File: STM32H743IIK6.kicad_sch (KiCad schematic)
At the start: 66 parts, among them Q2 MMBT3904, Q3 MMBT3904, SW1 SW_Push, SW2 SW_Push, SW3 SW_Push, SW4 SW_Push, U11 TLV75733PDBV, U2 STM32H743IITx, U8 TLV75733PDBV, Y1 25MHz, Y2 32.768KHz

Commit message: not yet
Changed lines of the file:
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@@
 	(hierarchical_label "DBG_RX"
 		(shape input)
-		(at 300.99 96.52 0)
+		(at 181.61 140.97 0)
 		(fields_autoplaced yes)
 		(effects
@@
 	(hierarchical_label "DBG_TX"
 		(shape output)
-		(at 300.99 93.98 0)
-		(fields_autoplaced yes)
-		(effects
+		(at 181.61 138.43 0)
+		(fields_autoplaced yes)
+		(effects

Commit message: Button, LED, i2s audio, LCD & SD ctrl left
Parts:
- added NT1, NT2, NT3: NetTie_2, NetTie:NetTie-2_SMD_Pad0.5mm, symbol Device:NetTie_2
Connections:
- net BCK is gone; now on net I2S_CK: U2.139 (PC10)
- net LRCK is gone; now on net LCD_BLK: U2.138 (PA15)
- net DBG_RX: now also U2.150 (PD6)
- net DBG_TX: now also U2.147 (PD5)
- net DCMI_HSYNC: now also U2.85 (PH8)
- net DCMI_PIXCLK: now also NT1.2
- net DCMI_VSYNC: now also U2.174 (PI5)
- net I2S_CK: no longer U2.51 (PA5)
- net I2S_SDO: now also U2.141 (PC12); no longer U2.151 (PD7)
- net LCD_BLK: no longer U2.163 (PB5)
- net LCD_CS: now also U2.132 (PI1), U2.7 (PI8)
- net LCD_DISP: now also U2.131 (PI0)
- net SD_DET: now also U2.2 (PE3)
- net LCD_SPI_CLK: now reaches U2.1 (PE2)
- net USART6_TX: now reaches U2.115 (PC6)
- net USART6_TX: now also NT2.1
- net USART6_RX: now reaches U2.116 (PC7)
- net USART6_RX: now also NT3.1
- net DCMI_D4: now reaches U2.129 (PH14)
- net DCMI_D5: now reaches U2.145 (PD3)
- net DCMI_D6: now reaches U2.175 (PI6)
- net DCMI_D7: now reaches U2.176 (PI7)
- net LCD_SPI_DAT: now reaches U2.5 (PE6)
- net LCD_SPI_MISO: now reaches U2.52 (PA6)
- net LCD_SPI_MISO: now also NT1.1
- net DCMI_D2: now reaches U2.88 (PH11)
- net DCMI_D3: now reaches U2.89 (PH12)
- new net DCMI_D0: NT2.2
- new net DCMI_D1: NT3.2
- new net LCD_SPI_MOSI: U2.163 (PB5)
- new net LCD_SPI_RESET: U2.151 (PD7)
- new net LCD_SPI_SCK: U2.51 (PA5)
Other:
- note added: "I2S3_CK > PC10"
- note added: "I2S3_SDO > PC12"
- note added: "I2S3_WS > PA4"
- moved on the sheet: BT2, C25, C26, C60, C61, C62, D11, D12, D7, R39, R40, R41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

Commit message: Almost finished
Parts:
- BT2: JLCPCB Part # (none) -> C964729
- Q2, Q3: JLCPCB Part # (none) -> C20526
- R22, R39: JLCPCB Part # C25741 -> C60491
- R50, R52: JLCPCB Part # C25741 -> C25744
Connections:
- net LCD_CS: no longer U2.7 (PI8)
- net LCD_SPI_DC: now also U2.134 (PI3)
- new net LCD_SPI_CS: U2.7 (PI8)
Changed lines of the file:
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@@
 		)
 	)
+	(hierarchical_label "LCD_SPI_CS"
+		(shape output)
+		(at 58.42 93.98 180)
+		(fields_autoplaced yes)
+		(effects
+			(font
+				(size 1.27 1.27)
+			)
+			(justify right)
+		)
+	)
 	(hierarchical_label "LCD_CS"
 		(shape input)
@@
 	(hierarchical_label "LCD_SPI_DC"
 		(shape output)
-		(at 234.95 86.36 180)
+		(at 58.42 81.28 180)
 		(fields_autoplaced yes)
 		(effects
@@
 		)
 	)
-	(hierarchical_label "LCD_CS"
-		(shape output)
-		(at 58.42 93.98 180)
-		(fields_autoplaced yes)
-		(effects
-			(font
-				(size 1.27 1.27)
-			)
-			(justify right)
-		)
-	)
 	(hierarchical_label "LCD_SPI_MISO"
 		(shape input)
@@
 			)
 		)
-		(property "JLCPCB Part #" "C25741"
+		(property "JLCPCB Part #" "C25744"
 			(at 252.73 266.7 0)
 			(effects
@@
 			)
 		)
+		(property "JLCPCB Part #" "C20526"
+			(at 264.16 212.09 0)
+			(effects
+				(font
+					(size 1.27 1.27)
+				)
+				(hide yes)
+			)
+		)
 		(pin "2"
 		)
@@
 			)
 		)
-		(property "JLCPCB Part #" "C25741"
+		(property "JLCPCB Part #" "C60491"
 			(at 308.61 124.46 0)
 			(effects
@@
 			)
 		)
-		(property "JLCPCB Part #" "C25741"
+		(property "JLCPCB Part #" "C25744"
 			(at 252.73 215.9 0)
 			(effects
@@
 			)
 		)
-		(property "JLCPCB Part #" "C25741"
+		(property "JLCPCB Part #" "C60491"
 			(at 308.61 168.91 0)
 			(effects
@@
 			)
 		)
+		(property "JLCPCB Part #" "C20526"
+			(at 264.16 262.89 0)
+			(effects
+				(font
+					(size 1.27 1.27)
+				)
+				(hide yes)
+			)
+		)
 		(pin "2"
 		)
@@
 				(hide yes)
 			)
+		)
+		(property "JLCPCB Part #" "C964729"
+			(at 207.01 54.61 0)
+			(effects
+				(font
+					(size 1.27 1.27)
+				)
+				(hide yes)
+			)

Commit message: Still on progress...
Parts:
- removed C45: 10uF/0805, Capacitor_SMD:C_0805_2012Metric, symbol Device:C
- removed D3: NSR0320MW2T1G, Diode_SMD:D_SOD-323, symbol Diode:NSR0340HT1G
- removed R22: 100K, Resistor_SMD:R_0402_1005Metric, symbol Device:R_Small
- removed R40: 10K, Resistor_SMD:R_0402_1005Metric, symbol Device:R_Small
- removed U11: TLV75733PDBV, Package_TO_SOT_SMD:SOT-23-5, symbol Regulator_Linear:TLV75733PDBV
- added U13: AMS1117-3.3, Package_TO_SOT_SMD:SOT-223-3_TabPin2, symbol Regulator_Linear:AMS1117-3.3
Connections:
- net +3V3: no longer C62.1, R41.1
- net BTN0: now also U2.99 (PD11)
- net BTN1: now also U2.84 (PH7)
- net GND: now also U13.1 (GND)
- net LCD_SPI_DC: now also U2.121 (PA10); no longer U2.134 (PI3)
- net LED_0: now also U2.55 (PC5)
- net LED_1: now also U2.83 (PH6)
- net VDD: now also U13.3 (VI)
- net I2S3_SD_MODE: now reaches U2.34 (PC2_C)
- net I2S2_WS: now reaches U2.92 (PB12)
- net I2S2_CK: now reaches U2.93 (PB13)
- net I2S_CK renamed I2S3_CK
- net I2S_SDO renamed I2S3_SDO
- net I2S_WS renamed I2S3_WS
- new net +3V3A: C62.1, R41.1, U13.2 (VO)
- new net I2S2_DIN: U2.134 (PI3)
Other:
- moved on the sheet: C60, C61, C62, D11, R39

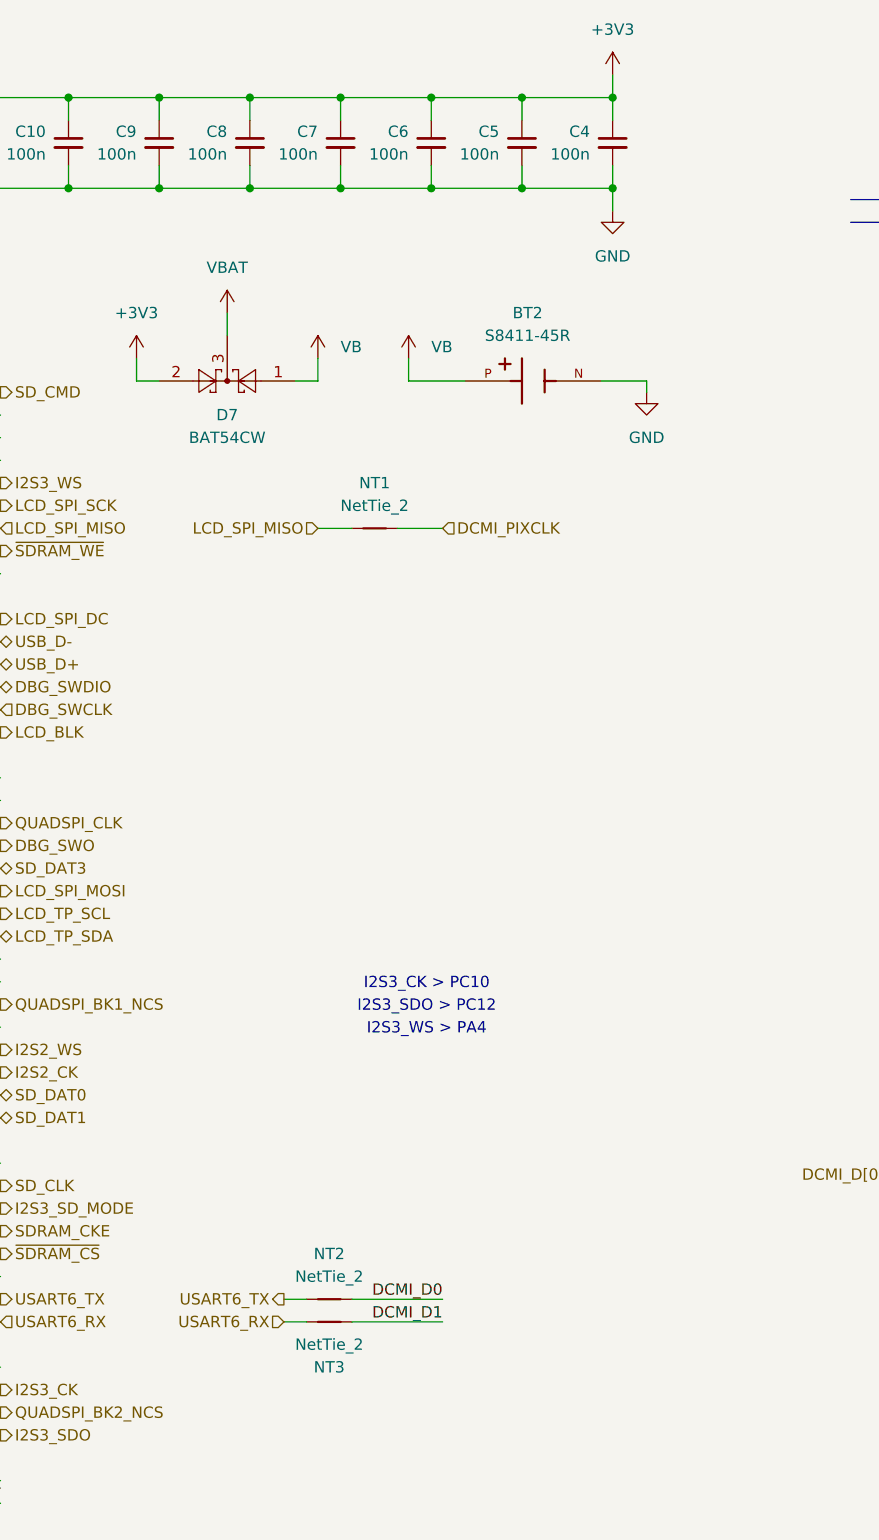
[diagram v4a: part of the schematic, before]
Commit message: Removing Camera, create alternative footprint for SPI LCD conn
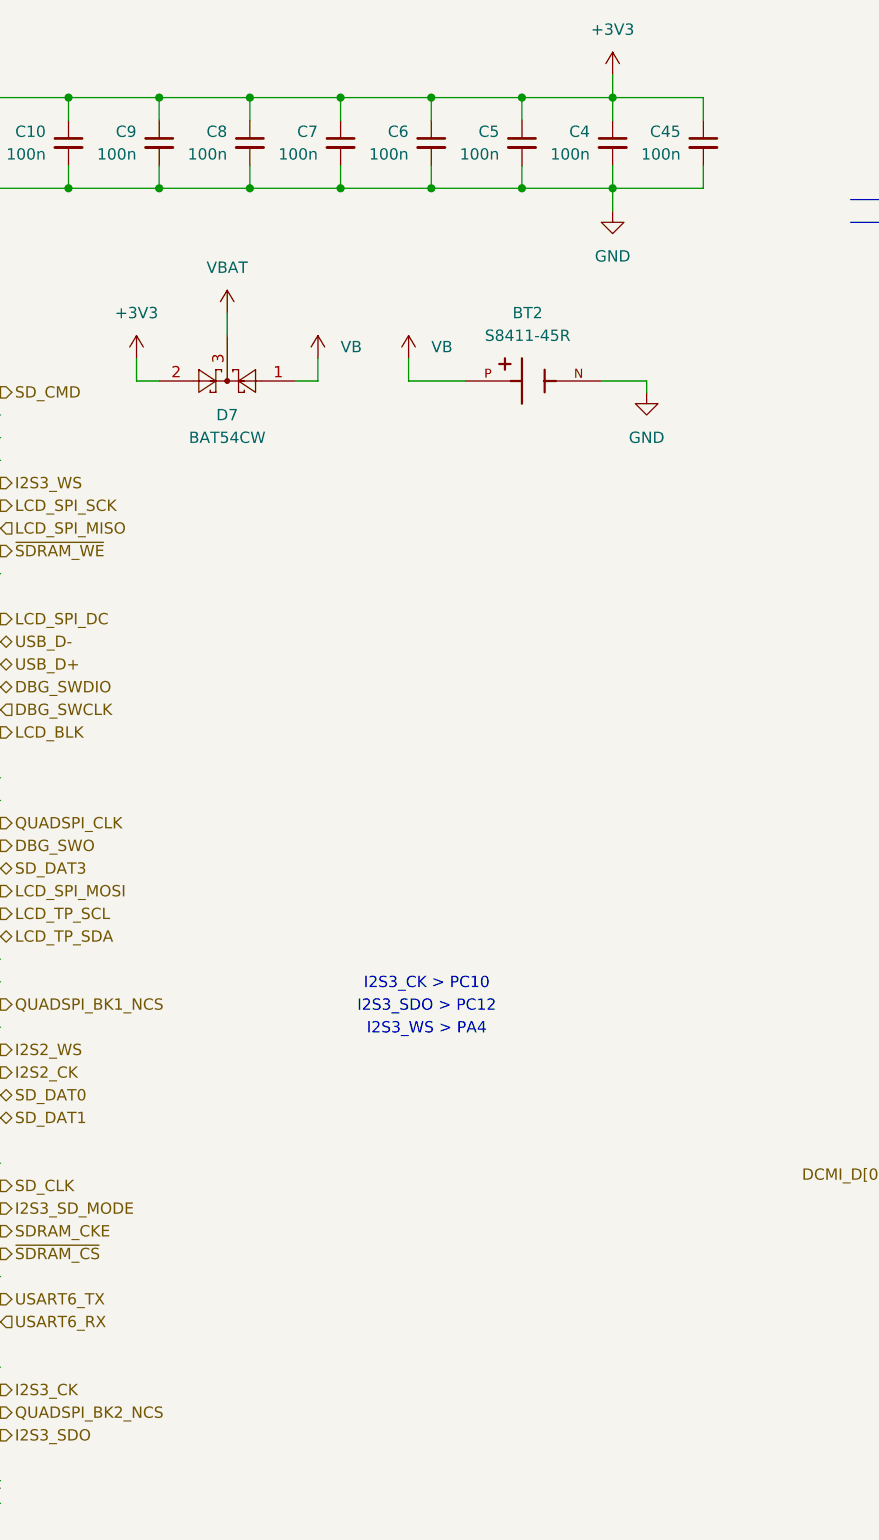
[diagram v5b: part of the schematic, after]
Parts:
- removed NT1, NT2, NT3: NetTie_2, NetTie:NetTie-2_SMD_Pad0.5mm, symbol Device:NetTie_2
- added C45: 100n, Capacitor_SMD:C_0402_1005Metric, symbol Device:C_Small
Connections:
- net +3V3: now also C45.1
- net GND: now also C45.2

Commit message: First release
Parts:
- added TP1, TP2, TP3, TP4: TestPoint, TestPoint:TestPoint_Pad_D1.5mm, symbol Connector:TestPoint
- U13: JLCPCB Part # (none) -> C6186
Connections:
- net +3V3: now also TP1.1
- net +3V3A: now also TP3.1
- net GND: now also TP2.1, TP4.1
- net DCMI_D4 renamed VBUS_EN
